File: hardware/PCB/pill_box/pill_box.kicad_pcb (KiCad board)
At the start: 2 copper layers, 22 parts, among them J1 MOTOR DRIVER 1, J10 Conn_01x15_Pin, J11 3.3v, J12 5v, J13 Conn_01x15_Pin, J2 MOTOR DRIVER 2, J3 MOTOR DRIVER 3, J4 SERVO MOTOR, J5 LED 1, J6 LED 2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

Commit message: made some wiring changes
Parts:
- moved R1 2.39 mm to (81.7, 61.5)
- moved R2 1.51 mm to (80.2, 69.0)
- moved R6 1.00 mm to (154.2, 87.5)
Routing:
- net GND: track 324.6 -> 337.7 mm
- net /D1(GPIO5): track 132.2 -> 130.1 mm
- net /D7(GPIO13): track 13.6 -> 14.7 mm
- net /D4(GPIO2): track 102.4 -> 103.4 mm
- net +3.3V: track 100.0 -> 99.1 mm
- net /D2(GPIO4): track 166.3 -> 165.5 mm
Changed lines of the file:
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@@
 	(footprint "Resistor_THT:R_Axial_DIN0207_L6.3mm_D2.5mm_P7.62mm_Horizontal"
 		(layer "F.Cu")
-		(at 80.38 63.5)
+		(at 81.69 61.5)
 		(descr "Resistor, Axial_DIN0207 series, Axial, Horizontal, pin pitch=7.62mm, 0.25W = 1/4W, length*diameter=6.3*2.5mm^2, http://cdn-reichelt.de/documents/datenblatt/B400/1_4W%23YAG.pdf")
 		(tags "Resistor Axial_DIN0207 series Axial Horizontal pin pitch 7.62mm 0.25W = 1/4W length 6.3mm diameter 2.5mm")
@@
 	(footprint "Resistor_THT:R_Axial_DIN0207_L6.3mm_D2.5mm_P7.62mm_Horizontal"
 		(layer "F.Cu")
-		(at 80.38 67.5)
+		(at 80.19 69)
 		(descr "Resistor, Axial_DIN0207 series, Axial, Horizontal, pin pitch=7.62mm, 0.25W = 1/4W, length*diameter=6.3*2.5mm^2, http://cdn-reichelt.de/documents/datenblatt/B400/1_4W%23YAG.pdf")
 		(tags "Resistor Axial_DIN0207 series Axial Horizontal pin pitch 7.62mm 0.25W = 1/4W length 6.3mm diameter 2.5mm")
@@
 	(footprint "Resistor_THT:R_Axial_DIN0207_L6.3mm_D2.5mm_P7.62mm_Horizontal"
 		(layer "F.Cu")
-		(at 155.19 87.5)
+		(at 154.19 87.5)
 		(descr "Resistor, Axial_DIN0207 series, Axial, Horizontal, pin pitch=7.62mm, 0.25W = 1/4W, length*diameter=6.3*2.5mm^2, http://cdn-reichelt.de/documents/datenblatt/B400/1_4W%23YAG.pdf")
 		(tags "Resistor Axial_DIN0207 series Axial Horizontal pin pitch 7.62mm 0.25W = 1/4W length 6.3mm diameter 2.5mm")
@@
 	)
 	(gr_line
-		(start 153 87.5)
-		(end 155.19 87.5)
-		(stroke
-			(width 0.2)
-			(type default)
-		)
-		(layer "F.Cu")
-		(net 38)
-	)
-	(gr_line
 		(start 185.5 114.5)
 		(end 55 114.5)
@@
 	)
 	(segment
-		(start 173.92 70.16)
-		(end 174 70.24)
-		(width 0.2)
-		(layer "F.Cu")
-		(net 13)
-	)
-	(segment
 		(start 159 93.54)
 		(end 158.54 94)
@@
 	)
 	(segment
+		(start 174 63)
+		(end 177 63)
+		(width 0.2)
+		(layer "F.Cu")
+		(net 13)
+	)
+	(segment
 		(start 158.54 84.5)
 		(end 158.54 75.5)
@@
 	)
 	(segment
-		(start 173.92 63.5)
-		(end 173.92 70.16)
-		(width 0.2)
-		(layer "F.Cu")
-		(net 13)
-	)
-	(segment
 		(start 158.54 94)
 		(end 158.54 84.5)
@@
 	)
 	(segment
+		(start 173.92 70.16)
+		(end 173.92 63.08)
+		(width 0.2)
+		(layer "F.Cu")
+		(net 13)
+	)
+	(segment
 		(start 71.69 90.2)
 		(end 68.07 90.2)
@@
 	)
 	(segment
-		(start 165.34 63)
-		(end 177 63)
+		(start 143.5 70.24)
+		(end 174 70.24)
 		(width 0.2)
 		(layer "F.Cu")
@@
 	)
 	(segment
-		(start 66.19 75)
-		(end 66.19 78)
+		(start 165.34 63)
+		(end 174 63)
 		(width 0.2)
 		(layer "F.Cu")
@@
 	)
 	(segment
-		(start 169.5 75.5)
-		(end 158.54 75.5)
+		(start 66.19 75)
+		(end 66.19 78)
 		(width 0.2)
 		(layer "F.Cu")
@@
 	)
 	(segment
-		(start 143.5 70.24)
-		(end 174 70.24)
+		(start 169.5 75.5)
+		(end 158.54 75.5)
 		(width 0.2)
 		(layer "F.Cu")
@@
 	)
 	(segment
+		(start 172.735 106)
+		(end 172.735 93.775)
+		(width 0.2)
+		(layer "F.Cu")
+		(net 13)
+	)
+	(segment
 		(start 71.69 77.5)
 		(end 71.69 90.2)
@@
 	)
 	(segment
+		(start 174 70.24)
+		(end 173.92 70.16)
+		(width 0.2)
+		(layer "F.Cu")
+		(net 13)
+	)
+	(segment
+		(start 172.735 93.775)
+		(end 172.5 93.54)
+		(width 0.2)
+		(layer "F.Cu")
+		(net 13)
+	)
+	(segment
 		(start 159 84.04)
 		(end 158.54 84.5)
@@
 	)
 	(segment
+		(start 173.92 63.08)
+		(end 174 63)
+		(width 0.2)
+		(layer "F.Cu")
+		(net 13)
+	)
+	(segment
 		(start 114.69 92.5)
 		(end 114.69 88.33)
@@
 	)
 	(segment
-		(start 162.81 87.5)
-		(end 169 87.5)
-		(width 0.2)
-		(layer "F.Cu")
-		(net 17)
-	)
-	(segment
 		(start 143.5 72.78)
 		(end 153.22 72.78)
@@
 	)
 	(segment
-		(start 169 87.5)
-		(end 172.5 91)
-		(width 0.2)
-		(layer "F.Cu")
-		(net 17)
-	)
-	(segment
 		(start 151.5 62.92)
 		(end 155.46 62.92)
@@
 	)
 	(segment
+		(start 161.81 87.5)
+		(end 169 87.5)
+		(width 0.2)
+		(layer "F.Cu")
+		(net 17)
+	)
+	(segment
 		(start 177 57.92)
 		(end 149 57.92)
@@
 	)
 	(segment
+		(start 169 87.5)
+		(end 172.5 91)
+		(width 0.2)
+		(layer "F.Cu")
+		(net 17)
+	)
+	(segment
 		(start 148.5 58.42)
 		(end 149 57.92)
@@
 	)
 	(segment
-		(start 88 67.5)
-		(end 88 75)
-		(width 0.2)
-		(layer "F.Cu")
-		(net 34)
-	)
-	(segment
-		(start 75.69 74.96)
-		(end 79.69 74.96)
+		(start 101 40.34)
+		(end 100.69 40.65)
 		(width 0.2)
 		(layer "F.Cu")
@@
 	)
 	(segment
-		(start 101 40.34)
-		(end 100.69 40.65)
+		(start 95.5 40.65)
+		(end 120.15 40.65)
 		(width 0.2)
 		(layer "F.Cu")
@@
 	)
 	(segment
-		(start 95.5 40.65)
-		(end 120.15 40.65)
+		(start 87.81 69)
+		(end 87.81 74.81)
 		(width 0.2)
 		(layer "F.Cu")
@@
 	)
 	(segment
-		(start 137.04 57.54)
-		(end 143.5 57.54)
+		(start 87.81 74.81)
+		(end 87.66 74.96)
 		(width 0.2)
 		(layer "F.Cu")
@@
 	)
 	(segment
-		(start 87.96 74.96)
-		(end 88 75)
+		(start 137.04 57.54)
+		(end 143.5 57.54)
 		(width 0.2)
 		(layer "F.Cu")
@@
 	)
 	(segment
-		(start 83.96 74.96)
-		(end 84 75)
-		(width 0.2)
-		(layer "F.Cu")
-		(net 34)
-	)
-	(segment
-		(start 83.69 74.96)
-		(end 87.96 74.96)
+		(start 87.66 74.96)
+		(end 75.69 74.96)
 		(width 0.2)
 		(layer "F.Cu")
@@
 	)
 	(segment
-		(start 79.69 74.96)
-		(end 83.96 74.96)
-		(width 0.2)
-		(layer "F.Cu")
-		(net 34)
-	)
-	(segment
 		(start 151.2 55)
 		(end 151.5 55.3)
@@
 	)
 	(segment
+		(start 88.85884 61.340255)
+		(end 110.030255 61.340255)
+		(width 0.2)
+		(layer "F.Cu")
+		(net 37)
+	)
+	(segment
 		(start 92.69 45.81)
 		(end 89 45.81)
@@
 	)
 	(segment
+		(start 110.030255 61.340255)
+		(end 110.19 61.5)
+		(width 0.2)
+		(layer "F.Cu")
+		(net 37)
+	)
+	(segment
 		(start 109.69 77.5)
 		(end 110.19 77)
@@
 	(segment
 		(start 110.19 63.5)
-		(end 110.19 43.19)
+		(end 110.19 61.5)
 		(width 0.2)
 		(layer "F.Cu")
@@
 	)
 	(segment
-		(start 88.69 45.5)
-		(end 88.69 43.19)
+		(start 110.19 61.5)
+		(end 110.19 43.19)
 		(width 0.2)
 		(layer "F.Cu")
@@
 	)
 	(segment
-		(start 86.505 43.19)
+		(start 88.69 45.5)
 		(end 88.69 43.19)
 		(width 0.2)
@@
 	)
 	(segment
-		(start 88 63.5)
-		(end 110.19 63.5)
+		(start 86.505 43.19)
+		(end 88.69 43.19)
 		(width 0.2)
 		(layer "F.Cu")
@@
 	)
 	(segment
+		(start 153.14 87.5)
+		(end 154.19 87.5)
+		(width 0.2)
+		(layer "F.Cu")
+		(net 38)
+	)
+	(segment
 		(start 143.5 77.86)
 		(end 153.14 87.5)
@@
 	)
 	(segment
-		(start 80.38 63.5)
-		(end 75.69 63.5)
-		(width 0.2)
-		(layer "F.Cu")
-		(net 41)
-	)
-	(segment
 		(start 68.07 72.42)
 		(end 71.61 72.42)
@@
 	)
 	(segment
-		(start 75.69 67.5)
-		(end 75.69 63.5)
-		(width 0.2)
-		(layer "F.Cu")
-		(net 41)
-	)
-	(segment
-		(start 83.08 38.11)
-		(end 82.69 38.5)
-		(width 0.2)
-		(layer "F.Cu")
-		(net 41)
-	)
-	(segment
 		(start 86.585 38.19)
 		(end 86.505 38.11)
@@
 	(segment
 		(start 82.69 57)
-		(end 82.69 38.5)
+		(end 80.5 59.19)
 		(width 0.2)
 		(layer "F.Cu")
@@
 	)
 	(segment
-		(start 71.69 69)
-		(end 71.69 67.5)
+		(start 86.505 38.11)
+		(end 83.08 38.11)
 		(width 0.2)
 		(layer "F.Cu")
@@
 	)
 	(segment
-		(start 75.69 72.42)
-		(end 75.69 67.5)
+		(start 82.69 38.5)
+		(end 82.69 57)
 		(width 0.2)
 		(layer "F.Cu")
@@
 	)
 	(segment
-		(start 80.38 59.31)
-		(end 82.69 57)
+		(start 80.5 60.31)
+		(end 81.69 61.5)
 		(width 0.2)
 		(layer "F.Cu")
@@
 	)
 	(segment
-		(start 80.38 63.5)
-		(end 80.38 59.31)
+		(start 75.69 72.42)
+		(end 75.69 61.5)
 		(width 0.2)
 		(layer "F.Cu")
@@
 	)
 	(segment
+		(start 75.69 61.5)
+		(end 81.69 61.5)
+		(width 0.2)
+		(layer "F.Cu")
+		(net 41)
+	)
+	(segment
 		(start 71.19 28.225)
 		(end 86.23 28.225)
@@
 	)
 	(segment
-		(start 76.38 71.73)
-		(end 75.69 72.42)
-		(width 0.2)
-		(layer "F.Cu")
-		(net 41)
-	)
-	(segment
-		(start 86.505 38.11)
-		(end 83.08 38.11)
+		(start 83.08 38.11)
+		(end 82.69 38.5)
 		(width 0.2)
 		(layer "F.Cu")
@@
 	)
 	(segment
-		(start 80.38 67.5)
-		(end 75.69 67.5)
+		(start 80.19 69)
+		(end 71.69 69)
 		(width 0.2)
 		(layer "F.Cu")
@@
 	)
 	(segment
-		(start 75.69 67.5)
-		(end 71.69 67.5)
+		(start 80.5 59.19)
+		(end 80.5 60.31)
 		(width 0.2)
 		(layer "F.Cu")

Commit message: capacitor
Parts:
- added C1: 100uF, Capacitor_THT:CP_Radial_D8.0mm_P3.50mm, F.Cu at (71.0, 27.3)
- added C2: 100uF, Capacitor_THT:CP_Radial_D8.0mm_P3.50mm, F.Cu at (174.7, 102.5)
- added C3: 0.1uF, Capacitor_THT:C_Disc_D5.0mm_W2.5mm_P2.50mm, F.Cu at (73.5, 97.5)
- added C4: 0.1uF, Capacitor_THT:C_Disc_D5.0mm_W2.5mm_P2.50mm, F.Cu at (71.5, 60.8)
- added C5: 0.1uF, Capacitor_THT:C_Disc_D5.0mm_W2.5mm_P2.50mm, F.Cu at (137.2, 100.5)
- J10: value Conn_01x15_Pin -> node mcu
- J13: value Conn_01x15_Pin -> node mcu_second
- moved J12 11.4 mm to (180.8, 96.0)
- moved J11 9.24 mm to (62.0, 27.2)
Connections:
- J13 pad 3: /D2(GPIO4) -> +3.3V
- R1 pad 2: /D2(GPIO4) -> +3.3V
- R3 pad 2: /D2(GPIO4) -> +3.3V
- U2 pad 14: /D2(GPIO4) -> +3.3V
- U3 pad 14: /D2(GPIO4) -> +3.3V
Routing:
- net +3.3V: track 99.1 -> 292.7 mm
- net /D2(GPIO4): track 165.5 -> 0.00 mm
- net GND: track 337.7 -> 391.9 mm
- net /3.3V: track 0.00 -> 12.5 mm
- net +5V: track 140.6 -> 148.3 mm

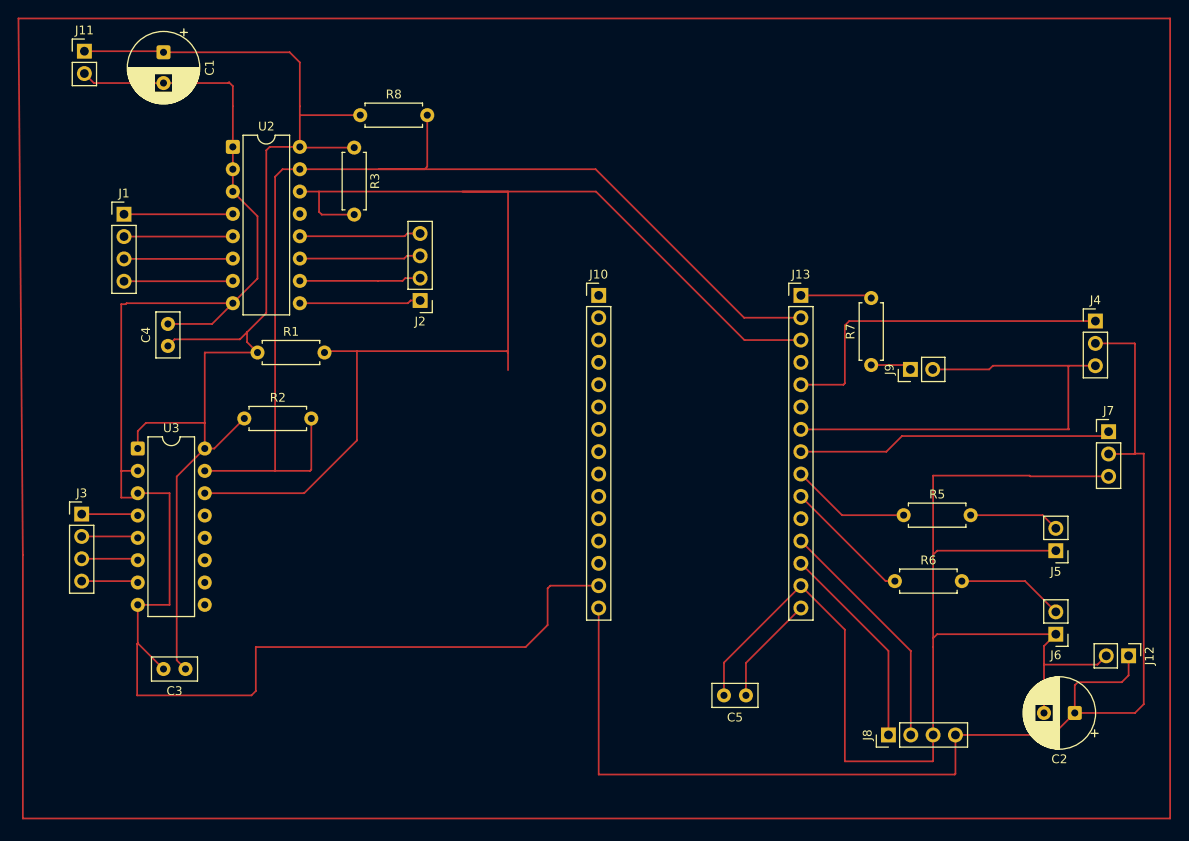
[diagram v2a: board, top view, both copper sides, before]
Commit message: pcb trace width increased
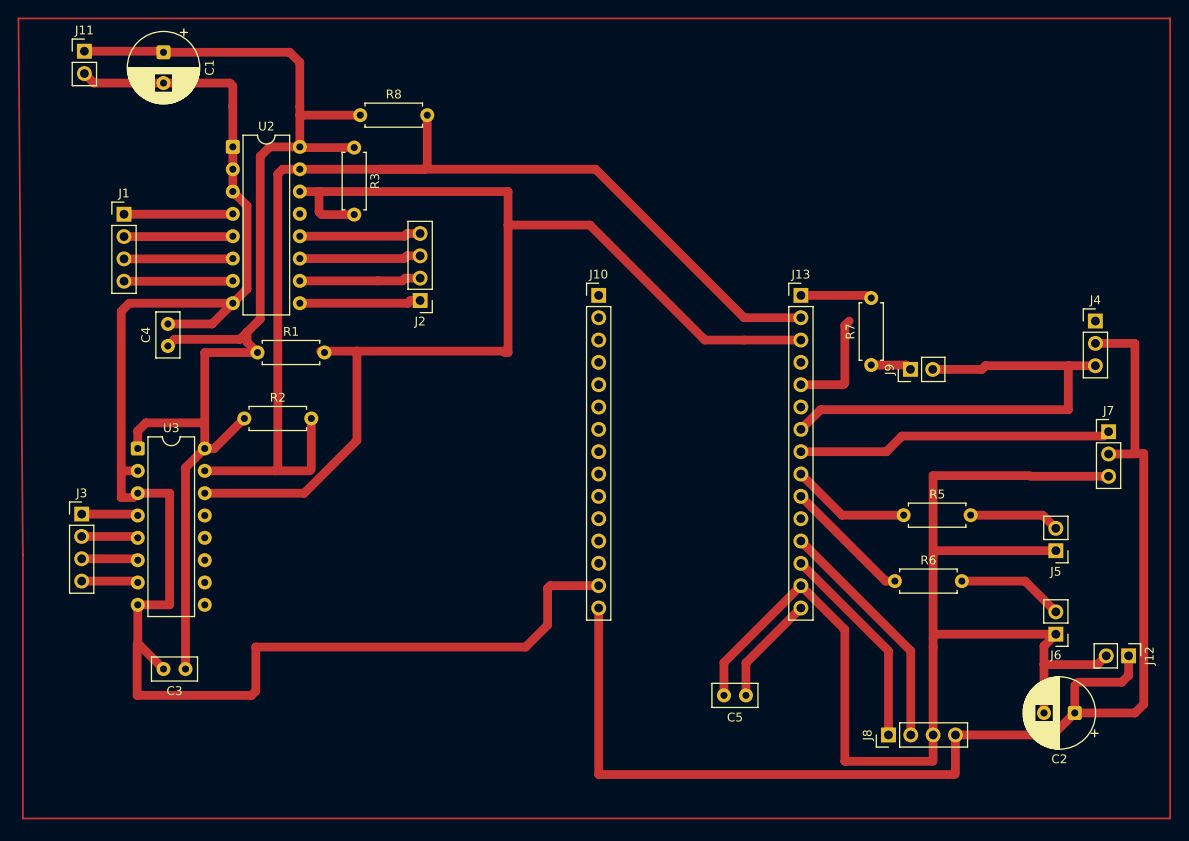
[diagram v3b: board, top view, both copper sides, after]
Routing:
- net +3.3V: track 292.7 -> 285.0 mm
- net GND: track 391.9 -> 389.6 mm

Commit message: checking commit
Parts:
- moved R1 1.58 mm to (80.2, 61.0)
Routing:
- net GND: track 389.6 -> 432.5 mm
- net +3.3V: track 285.0 -> 278.1 mm
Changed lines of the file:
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@@
 	(footprint "Resistor_THT:R_Axial_DIN0207_L6.3mm_D2.5mm_P7.62mm_Horizontal"
 		(layer "F.Cu")
-		(at 81.69 61.5)
+		(at 80.19 61)
 		(descr "Resistor, Axial_DIN0207 series, Axial, Horizontal, pin pitch=7.62mm, 0.25W = 1/4W, length*diameter=6.3*2.5mm^2, http://cdn-reichelt.de/documents/datenblatt/B400/1_4W%23YAG.pdf")
 		(tags "Resistor Axial_DIN0207 series Axial Horizontal pin pitch 7.62mm 0.25W = 1/4W length 6.3mm diameter 2.5mm")
@@
 	)
 	(segment
-		(start 171.152651 94.887349)
-		(end 172.5 93.54)
+		(start 61 40.65)
+		(end 78.885 40.65)
 		(width 1)
 		(layer "F.Cu")
@@
 	)
 	(segment
-		(start 81.5 100)
-		(end 81 100.5)
+		(start 171.152651 94.887349)
+		(end 172.5 93.54)
 		(width 1)
 		(layer "F.Cu")
@@
 	)
 	(segment
-		(start 80.5 44.805)
-		(end 80.5 54.275)
+		(start 81.5 100)
+		(end 81 100.5)
 		(width 1)
 		(layer "F.Cu")
@@
 	)
 	(segment
+		(start 61 57)
+		(end 61 40.65)
+		(width 1)
+		(layer "F.Cu")
+		(net 13)
+	)
+	(segment
 		(start 78.537349 30.847349)
 		(end 78.885 31.195)
@@
 	)
 	(segment
+		(start 58 71)
+		(end 58 90.5)
+		(width 1)
+		(layer "F.Cu")
+		(net 13)
+	)
+	(segment
 		(start 78.885 33.5)
 		(end 78.885 38.11)
@@
 	)
 	(segment
+		(start 66.19 56.81)
+		(end 61.19 56.81)
+		(width 1)
+		(layer "F.Cu")
+		(net 13)
+	)
+	(segment
 		(start 169.58 75.58)
 		(end 178.5 75.58)
@@
 	)
 	(segment
-		(start 66.19 78)
-		(end 67.57 78)
+		(start 61.19 56.81)
+		(end 61 57)
 		(width 1)
 		(layer "F.Cu")
@@
 	)
 	(segment
-		(start 80.5 54.275)
-		(end 78.885 55.89)
+		(start 66.19 78)
+		(end 67.57 78)
 		(width 1)
 		(layer "F.Cu")
@@
 	)
 	(segment
+		(start 66.19 71)
+		(end 66.19 56.81)
+		(width 1)
+		(layer "F.Cu")
+		(net 13)
+	)
+	(segment
 		(start 158.54 84.5)
 		(end 158.54 75.5)
@@
 	)
 	(segment
+		(start 66.19 71)
+		(end 58 71)
+		(width 1)
+		(layer "F.Cu")
+		(net 13)
+	)
+	(segment
 		(start 78.885 31.195)
 		(end 78.885 33.5)
@@
 	)
 	(segment
-		(start 71.69 90.2)
-		(end 68.07 90.2)
-		(width 1)
-		(layer "F.Cu")
-		(net 13)
-	)
-	(segment
 		(start 158.54 107.96)
 		(end 158.5 108)
@@
 	)
 	(segment
-		(start 68.07 77.5)
-		(end 71.69 77.5)
-		(width 1)
-		(layer "F.Cu")
-		(net 13)
-	)
-	(segment
 		(start 158.5 63.42)
 		(end 164.08 63.42)
@@
 	(segment
 		(start 66.19 75)
-		(end 66.19 56.81)
-		(width 1)
-		(layer "F.Cu")
-		(net 13)
-	)
-	(segment
-		(start 71.69 77.5)
-		(end 71.69 90.2)
+		(end 66.19 71)
 		(width 1)
 		(layer "F.Cu")
@@
 	)
 	(segment
-		(start 78.885 43.19)
-		(end 80.5 44.805)
+		(start 58.3 90.2)
+		(end 68.07 90.2)
 		(width 1)
 		(layer "F.Cu")
@@
 	)
 	(segment
-		(start 84 41.19)
-		(end 84 74.65)
-		(width 1)
-		(layer "F.Cu")
-		(net 34)
-	)
-	(segment
-		(start 86.505 40.65)
-		(end 84.54 40.65)
-		(width 1)
-		(layer "F.Cu")
-		(net 34)
-	)
-	(segment
 		(start 101 40.34)
 		(end 100.69 40.65)
@@
 	)
 	(segment
-		(start 84 74.65)
-		(end 83.69 74.96)
+		(start 84.35 40.65)
+		(end 83.5 41.5)
 		(width 1)
 		(layer "F.Cu")
@@
 	)
 	(segment
+		(start 83.5 41.5)
+		(end 83.5 74.96)
+		(width 1)
+		(layer "F.Cu")
+		(net 34)
+	)
+	(segment
 		(start 137.04 57.54)
 		(end 143.5 57.54)
@@
 	)
 	(segment
-		(start 84.54 40.65)
-		(end 84 41.19)
+		(start 87.66 74.96)
+		(end 83.5 74.96)
 		(width 1)
 		(layer "F.Cu")
@@
 	)
 	(segment
-		(start 87.66 74.96)
+		(start 83.5 74.96)
 		(end 75.69 74.96)
 		(width 1)
@@
 	)
 	(segment
+		(start 86.505 40.65)
+		(end 84.35 40.65)
+		(width 1)
+		(layer "F.Cu")
+		(net 34)
+	)
+	(segment
 		(start 151.2 55)
 		(end 151.5 55.3)
@@
 	)
 	(segment
-		(start 86.505 38.11)
-		(end 83.08 38.11)
-		(width 1)
-		(layer "F.Cu")
-		(net 40)
-	)
-	(segment
-		(start 88.85884 61.340255)
-		(end 93 61.340255)
+		(start 92.69 45.81)
+		(end 89 45.81)
 		(width 1)
 		(layer "F.Cu")
@@
 	)
 	(segment
-		(start 92.69 45.81)
-		(end 89 45.81)
+		(start 109.849745 61.5)
+		(end 109.69 61.340255)
 		(width 1)
 		(layer "F.Cu")
@@
 	)
 	(segment
-		(start 109.849745 61.5)
-		(end 109.69 61.340255)
+		(start 80.19 61)
+		(end 80.19 59.5)
 		(width 1)
 		(layer "F.Cu")
@@
 	)
 	(segment
-		(start 82 57.69)
-		(end 80.5 59.19)
+		(start 83.08 38.11)
+		(end 81.5 39.69)
 		(width 1)
 		(layer "F.Cu")
@@
 	)
 	(segment
-		(start 93.38 34.5)
-		(end 86.505 34.5)
+		(start 92 61)
+		(end 87.81 61)
 		(width 1)
 		(layer "F.Cu")
@@
 	)
 	(segment
-		(start 82 39.19)
-		(end 82 57.69)
+		(start 93.38 34.5)
+		(end 86.505 34.5)
 		(width 1)
 		(layer "F.Cu")
@@
 	)
 	(segment
+		(start 86.505 38.11)
+		(end 83.08 38.11)
+		(width 1)
+		(layer "F.Cu")
+		(net 40)
+	)
+	(segment
 		(start 110.19 47)
 		(end 110.19 61.5)
@@
 	)
 	(segment
-		(start 105 43.19)
-		(end 105.88 43.19)
-		(width 0.2)
-		(layer "F.Cu")
-		(net 40)
-	)
-	(segment
 		(start 75.69 77.5)
 		(end 87 77.5)
@@
 	)
 	(segment
-		(start 80.5 60.31)
-		(end 81.69 61.5)
-		(width 1)
-		(layer "F.Cu")
-		(net 40)
-	)
-	(segment
-		(start 83.08 38.11)
-		(end 82 39.19)
-		(width 1)
-		(layer "F.Cu")
-		(net 40)
-	)
-	(segment
 		(start 75.69 69.5)
 		(end 75.69 61.5)
@@
 	)
 	(segment
-		(start 75.69 61.5)
-		(end 81.69 61.5)
+		(start 80.19 59.5)
+		(end 81.5 58.19)
 		(width 1)
 		(layer "F.Cu")
@@
 	)
 	(segment
+		(start 75.69 61.5)
+		(end 75 61.5)
+		(width 1)
+		(layer "F.Cu")
+		(net 40)
+	)
+	(segment
 		(start 86.505 43.19)
 		(end 88.69 43.19)
@@
 	)
 	(segment
-		(start 79.69 60)
-		(end 80.5 59.19)
+		(start 74.25 60.75)
+		(end 71.5 60.75)
+		(width 1)
+		(layer "F.Cu")
+		(net 40)
+	)
+	(segment
+		(start 75 61.5)
+		(end 74.25 60.75)
 		(width 1)
 		(layer "F.Cu")
@@
 	)
 	(segment
-		(start 72.25 60)
-		(end 79.69 60)
+		(start 75.69 61.5)
+		(end 76.19 61)
 		(width 1)
 		(layer "F.Cu")
@@
 	)
 	(segment
-		(start 80.5 59.19)
-		(end 80.5 60.31)
+		(start 81.5 39.69)
+		(end 81.5 58.19)
+		(width 1)
+		(layer "F.Cu")
+		(net 40)
+	)
+	(segment
+		(start 92.340255 61.340255)
+		(end 92 61)
+		(width 1)
+		(layer "F.Cu")
+		(net 40)
+	)
+	(segment
+		(start 76.19 61)
+		(end 80.19 61)
 		(width 1)
 		(layer "F.Cu")
@@
 	)
 	(segment
-		(start 71.5 60.75)
-		(end 72.25 60)
+		(start 85.352349 27.347349)
+		(end 86.505 28.5)
 		(width 1)
 		(layer "F.Cu")
@@
 	)
 	(segment
-		(start 85.352349 27.347349)
-		(end 86.505 28.5)
+		(start 93 61.340255)
+		(end 92.340255 61.340255)
 		(width 1)
 		(layer "F.Cu")
 		(net 40)
+	)
+	(segment
+		(start 106 43.19)
+		(end 105.88 43.19)
+		(width 0.2)
+		(layer "F.Cu")
+		(net 40)

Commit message: added changes
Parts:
- moved C3 11.2 mm to (84.5, 99.6)
- moved J2 11.2 mm to (111.2, 57.6)
- moved J3 11.2 mm to (72.7, 81.9)
- moved R1 11.2 mm to (91.2, 63.1)
- moved R2 11.2 mm to (91.2, 71.1)
- moved R3 11.2 mm to (103.7, 40.2)
- moved U2 11.2 mm to (89.9, 40.2)
- moved U3 11.2 mm to (79.1, 74.5)
- moved C1 11.2 mm to (82.0, 29.4)
- moved J1 11.2 mm to (77.5, 47.8)
- moved J11 11.2 mm to (73.0, 29.3)
- moved C4 10.9 mm to (81.5, 65.0)
- moved R8 10.9 mm to (104.2, 33.5)
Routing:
- net +3.3V: track 278.1 -> 264.2 mm
- net /D1(GPIO5): track 130.3 -> 118.1 mm
- net GND: track 432.5 -> 440.3 mm
